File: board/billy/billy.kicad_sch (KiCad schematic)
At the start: 85 parts, among them J1 Screw_Terminal_01x02, J10 Screw_Terminal_01x02, J11 Screw_Terminal_01x03, J12 USB_B_Micro, J2 Conn_01x06, J3 Screw_Terminal_01x02, J4 Screw_Terminal_01x02, J5 Conn_01x02, J6 Conn_01x03, J7 Screw_Terminal_01x02, J8 Screw_Terminal_01x02, J9 Screw_Terminal_01x02, Q1 AOSS32334C, Q2 AOSS32334C, Q3 AOSS32334C, Q4 AOSS32334C, SW1 TS-1088-AR02016, U1 ESP32-S3-WROOM-1, U2 DRV8833PWPR, U3 MAX98357A, U4 DRV8833PWPR, U5 LM74700-Q1, U6 AP63201WU, U7 USBLC6-2SC6, U8 LM74700-Q1, U9 LM74700-Q1

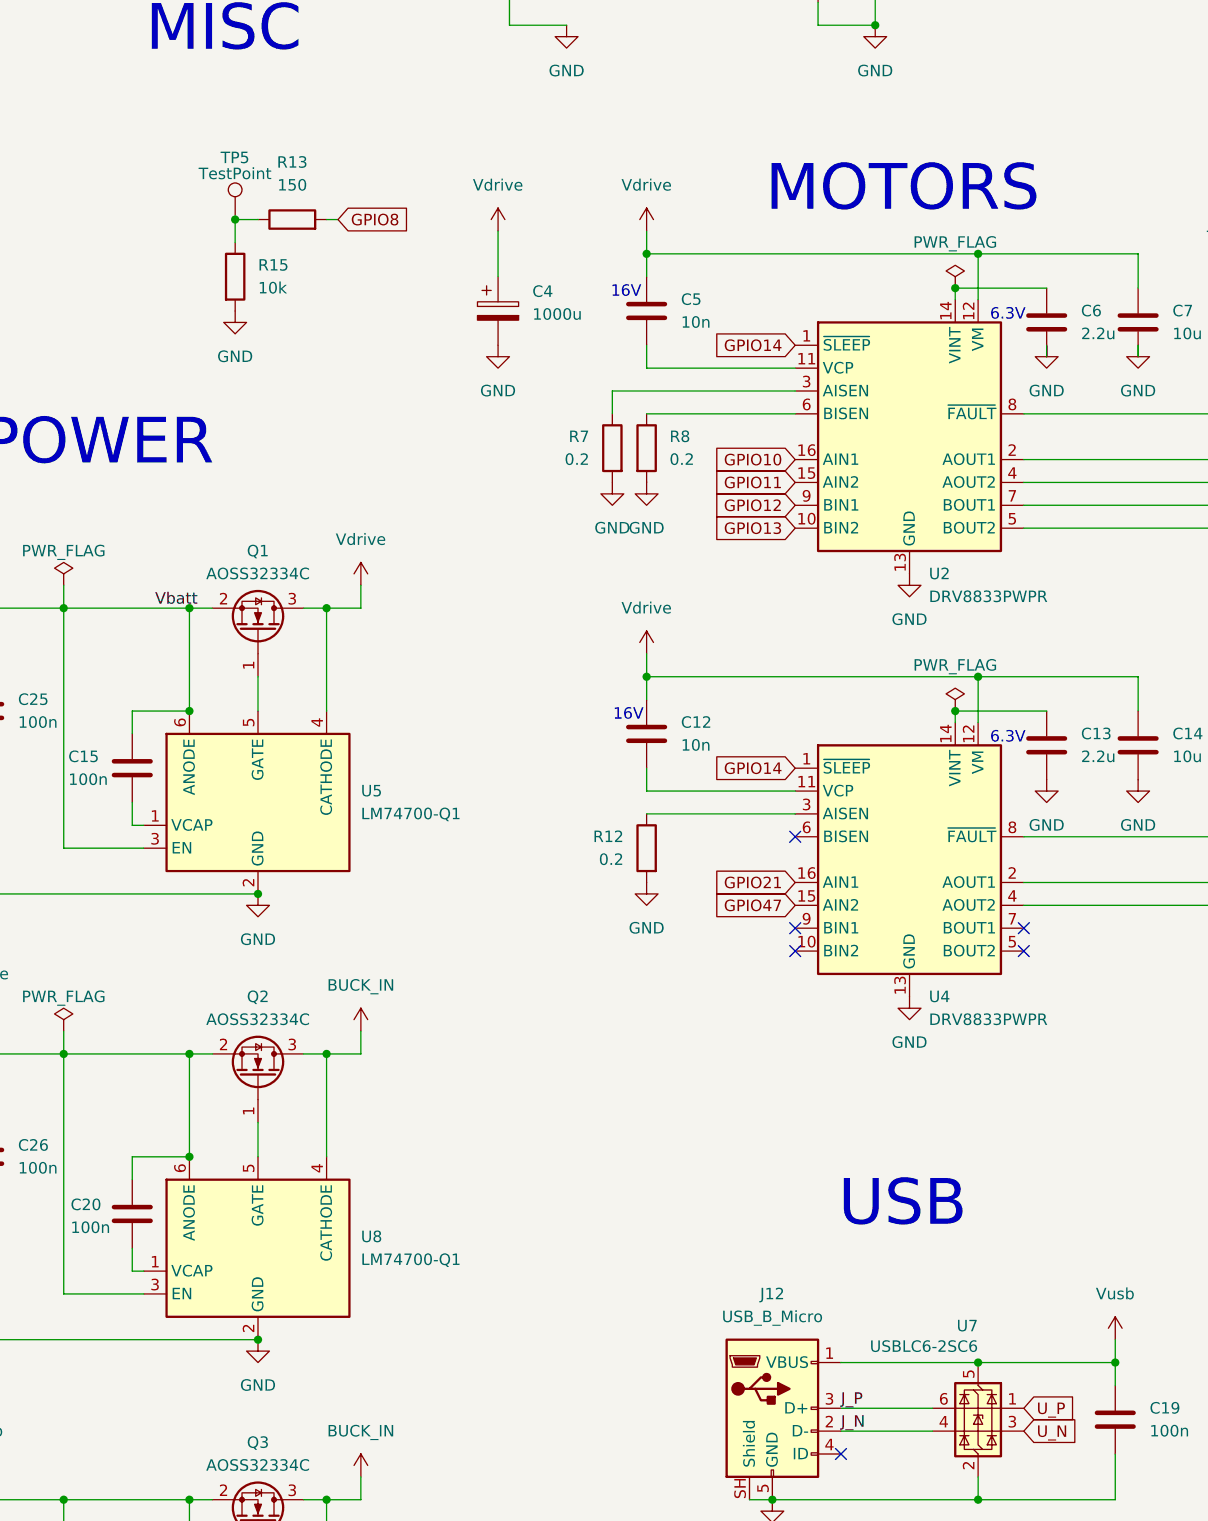
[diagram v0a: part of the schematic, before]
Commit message: Replace bare-pin misc probe (J13) with Keystone 5011 loop test point (TP5)
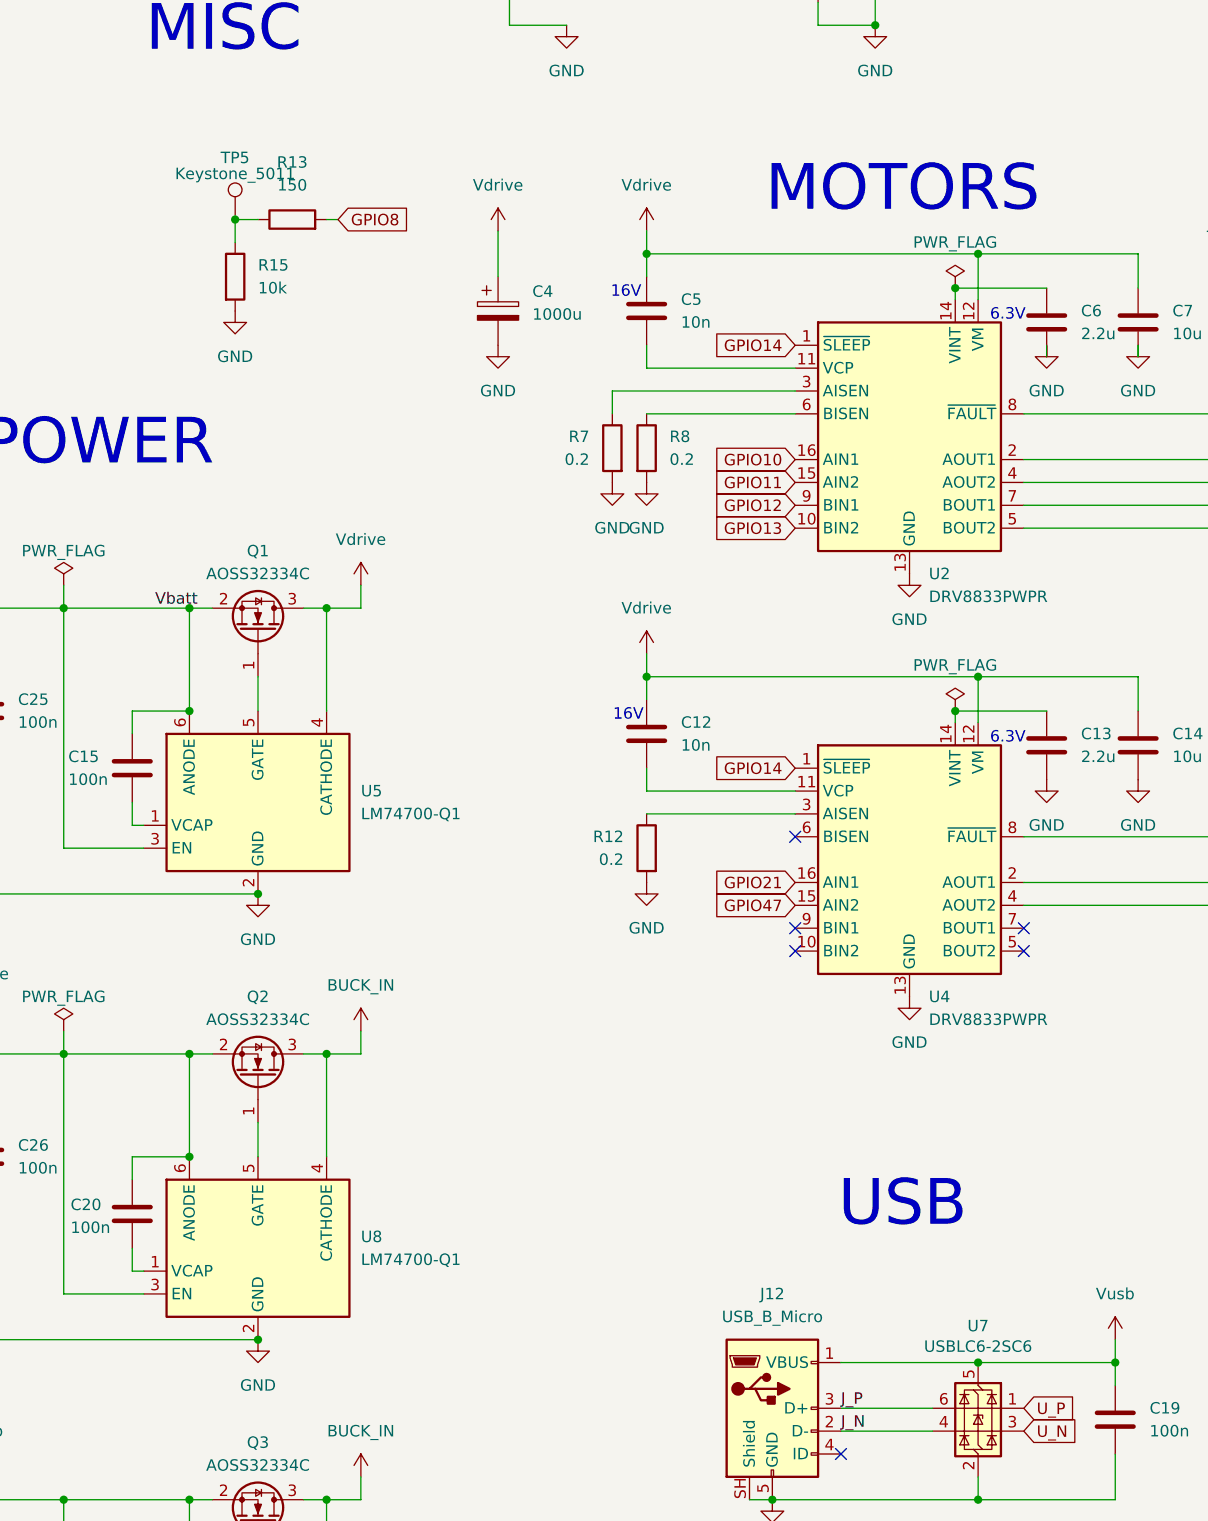
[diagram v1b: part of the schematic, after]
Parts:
- C1, C2, C3: DigiKey MF (none) -> Samsung Electro-Mechanics; DigiKey MP (none) -> CL05A105KA5NQNC
- C12, C5: DigiKey MF (none) -> Samsung Electro-Mechanics; DigiKey MP (none) -> CL05B103KB5NNNC
- C13, C6: DigiKey MF (none) -> Samsung Electro-Mechanics; DigiKey MP (none) -> CL10A225KO8NNNC
- C14, C7, C8: DigiKey MF (none) -> Samsung Electro-Mechanics; DigiKey MP (none) -> CL10A106KP8NNNC
- C15, C18, C19, C20, C21, C22, C25, C26, C27, C9: DigiKey MF (none) -> Samsung Electro-Mechanics; DigiKey MP (none) -> CL05B104KO5NNNC
- C16, C24: DigiKey MP CL21A226MAYNNWE -> CL21A226MAQNNNE
- C17: DigiKey MF (none) -> Samsung Electro-Mechanics; DigiKey MP (none) -> CL21A226MAQNNNE
- C4: DigiKey MF (none) -> PANASONIC; DigiKey MP (none) -> EEEFT1E102UP
- F1, F2: DigiKey MF (none) -> Littelfuse; DigiKey MP (none) -> 0154005.DRT
- J12: DigiKey MF (none) -> Amphenol ICC; DigiKey MP (none) -> 10118194-0001LF
- L1, L2: DigiKey MF (none) -> muRata; DigiKey MP (none) -> BLM18PG121SN1D
- Q1, Q2, Q3, Q4: DigiKey MF (none) -> AOS; DigiKey MP (none) -> AOSS32334C
- TP5: value TestPoint -> Keystone_5011; DigiKey MF (none) -> Keystone Electronics; DigiKey MP (none) -> 5011; DigiKey Part (none) -> 36-5011-ND; LCSC Part (none) -> C238127; MF (none) -> Keystone Electronics; MP (none) -> 5011
- U1: DigiKey MF (none) -> ESPRESSIF; DigiKey MP (none) -> ESP32-S3-WROOM-1-N4R2
- U2, U4: DigiKey MF (none) -> TI; DigiKey MP (none) -> DRV8833PWPR
- U3: DigiKey MF (none) -> MAXIM; DigiKey MP (none) -> MAX98357AETE+T
- U6: DigiKey MF (none) -> DIODES; DigiKey MP (none) -> AP63201WU-7
- U7: DigiKey MF (none) -> ST; DigiKey MP (none) -> USBLC6-2SC6

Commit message: Add part numbers for LM74700-Q1
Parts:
- U5, U8, U9: DigiKey MF (none) -> TI; DigiKey MP (none) -> LM74700QDBVTQ1; DigiKey Part (none) -> 296-53420-1-ND; LCSC Part (none) -> C2653623; MF (none) -> TI; MP (none) -> LM74700QDBVTQ1; Mouser MF (none) -> TI; Mouser MP (none) -> LM74700QDBVTQ1; Mouser Part (none) -> 595-LM74700QDBVTQ1

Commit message: Change some part numbers to active / in stock parts
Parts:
- C14, C7, C8: DigiKey MP CL10A106KP8NNNC -> CL10A106KP8NNND
- C16, C17, C24: DigiKey MP CL21A226MAQNNNE -> CL21A226KOQNNNG
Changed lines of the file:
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@@
 			)
 		)
-		(property "DigiKey MP" "CL10A106KP8NNNC"
+		(property "DigiKey MP" "CL10A106KP8NNND"
 			(at 256.54 97.79 0)
 			(hide yes)
@@
 			)
 		)
-		(property "DigiKey MP" "CL10A106KP8NNNC"
+		(property "DigiKey MP" "CL10A106KP8NNND"
 			(at 256.54 144.78 0)
 			(hide yes)
@@
 			)
 		)
-		(property "DigiKey MP" "CL10A106KP8NNNC"
+		(property "DigiKey MP" "CL10A106KP8NNND"
 			(at 330.2 110.49 0)
 			(hide yes)
@@
 			)
 		)
-		(property "DigiKey MP" "CL21A226MAQNNNE"
+		(property "DigiKey MP" "CL21A226KOQNNNG"
 			(at 309.88 201.93 0)
 			(hide yes)
@@
 			)
 		)
-		(property "DigiKey MP" "CL21A226MAQNNNE"
+		(property "DigiKey MP" "CL21A226KOQNNNG"
 			(at 379.73 201.93 0)
 			(hide yes)
@@
 			)
 		)
-		(property "DigiKey MP" "CL21A226MAQNNNE"
+		(property "DigiKey MP" "CL21A226KOQNNNG"
 			(at 391.16 201.93 0)
 			(hide yes)

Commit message: Open board rev.1, move over to using AP63203 part
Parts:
- removed C23: 100p, Capacitor_SMD:C_0402_1005Metric, symbol Device:C
- removed R14: 75k, Resistor_SMD:R_0603_1608Metric, symbol Device:R
- removed R16: 24k, Resistor_SMD:R_0603_1608Metric, symbol Device:R
- F1, F2: Mouser MF (none) -> Littelfuse; Mouser MP (none) -> 0154005.DRT; Mouser Part (none) -> 576-0154005.DRT
- J12: Mouser MF (none) -> Amphenol ICC; Mouser MP (none) -> 10118194-0001LF; Mouser Part (none) -> 649-10118194-0001LF
- L3: value 6.8u -> 3.3u; DigiKey MP TYA40206R8M-10 -> TYA40203R3M-10; DigiKey Part (none) -> 240-TYA40203R3M-10CT-ND; LCSC Part C6364812 -> (none); MF APV -> (none); MP ANR4030T6R8M -> (none); Mouser MF (none) -> Laird-Signal Integrity Products; Mouser MP (none) -> TYA40203R3M-10; Mouser Part (none) -> 739-TYA40203R3M-10
- TP5: Mouser MF (none) -> Keystone Electronics; Mouser MP (none) -> 5011; Mouser Part (none) -> 534-5011
- U6: value AP63201WU -> AP63203WU; symbol Regulator_Switching:AP63201WU -> Regulator_Switching:AP63203WU; DigiKey MP AP63201WU-7 -> AP63203WU-7; DigiKey Part (none) -> AP63203WU-7DICT-ND; LCSC Part C2071044 -> C780769; MP AP63201WU-7 -> AP63203WU-7; Mouser MF (none) -> DIODES; Mouser MP (none) -> AP63203QWU-7; Mouser Part (none) -> 621-AP63203QWU-7
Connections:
- net +3.3V: now also U6.1 (FB)
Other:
- note removed: "NOTE: We prefer AP63203 if available. If selected: 1. Remove 100p feed-forward cap 2. Remove voltage dividing resistors 3. Connect FB directly to +3.3V out 4. Inductor value 4.7uH"
- moved on the sheet: C16, C17, C22, C24, L3, U6

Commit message: Add Vmotor-sense divider on GPIO8 (R13/R15), shared across N8R8 dev and N4R2 main boards
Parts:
- removed TP5: Keystone_5011, TestPoint:TestPoint_Keystone_5010-5014_Multipurpose, symbol Connector:TestPoint
- R13: value 150 -> 100k; DigiKey MP RMCF0603FT150R -> RMCF0603FT100K; LCSC Part C22808 -> C25803; MP 0603WAF1500T5E -> 0603WAF1003T5E
- R15: value 10k -> 75k; DigiKey MP RMCF0603FT10K0 -> RMCF0603JT75K0; LCSC Part C25804 -> (none); MF UNI-ROYAL -> (none); MP 0603WAF1002T5E -> (none)
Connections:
- net GPIO8: now also R13.1, R15.1; no longer R13.2
- net Vdrive: now also R13.2
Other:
- note added: "V SENSE"
- note removed: "MISC"
- moved on the sheet: R13, R15

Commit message: Cleaned up the parts table and added Digikey and Mouser part numbers for all parts
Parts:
- C1, C2, C3: Attributes (none) -> 10% 25V X5R; DigiKey MF Samsung Electro-Mechanics -> (none); DigiKey MP CL05A105KA5NQNC -> (none); DigiKey Part (none) -> 1276-1445-1-ND; Mouser Part (none) -> 187-CL05A105KA5NQNC
- C10, C11: Attributes (none) -> 10% 50V X7R; DigiKey MF Vishay Vitramon -> (none); DigiKey MP VJ0402Y221KXACW1BC -> (none); DigiKey Part (none) -> 720-1616-1-ND; MF FH -> Vishay Vitramon; MP 0402B221K500NT -> VJ0402Y221KXACW1BC; Mouser Part (none) -> 77-VJ0402Y221KXACBC
- C12, C5: Attributes (none) -> 10% 50V X7R; DigiKey MF Samsung Electro-Mechanics -> (none); DigiKey MP CL05B103KB5NNNC -> (none); DigiKey Part (none) -> 1276-1028-1-ND; Mouser Part (none) -> 187-CL05B103KB5NNNC
- C13, C6: Attributes (none) -> 10% 16V X5R; DigiKey MF Samsung Electro-Mechanics -> (none); DigiKey MP CL10A225KO8NNNC -> (none); DigiKey Part (none) -> 1276-1040-1-ND; Mouser Part (none) -> 187-CL10A225KO8NNNC
- C14, C7, C8: Attributes (none) -> 10% 16V X5R; DigiKey MF Samsung Electro-Mechanics -> (none); DigiKey MP CL10A106KP8NNND -> (none); DigiKey Part (none) -> 1276-CL10A106KO8NQNCCT-ND; MP CL10A106KP8NNNC -> CL10A106KO8NQNC; Mouser Part (none) -> 187-CL10A106KO8NQNC
- C15, C18, C19, C20, C21, C22, C25, C26, C27, C9: Attributes (none) -> 10% 16V X7R; DigiKey MF Samsung Electro-Mechanics -> (none); DigiKey MP CL05B104KO5NNNC -> (none); DigiKey Part (none) -> 1276-1001-1-ND; Mouser Part (none) -> 187-CL05B104KO5NNNC
- C16, C17, C24: Attributes (none) -> 10% 16V X5R; DigiKey MF Samsung Electro-Mechanics -> (none); DigiKey MP CL21A226KOQNNNG -> (none); DigiKey Part (none) -> 1276-7092-1-ND; Mouser Part (none) -> 187-CL21A226MAQNNNE
- C4: Attributes (none) -> 20% 25V; DigiKey MF PANASONIC -> (none); DigiKey MP EEEFT1E102UP -> (none); DigiKey Part (none) -> P122428CT-ND; Mouser Part (none) -> 667-EEE-FT1E102UP
- D1: DigiKey MF SparkFun -> (none); DigiKey MP 16347 -> (none); DigiKey Part (none) -> 1568-16347CT-ND; MF Worldsemi -> SparkFun; MP WS2812B-V6 -> 16347
- F1, F2: DigiKey MF Littelfuse -> (none); DigiKey MP 0154005.DRT -> (none); DigiKey Part (none) -> F1310CT-ND
- J1, J10, J3, J4, J7, J8, J9: DigiKey MF Phoenix Contact -> (none); DigiKey MP 1725656 -> (none); DigiKey Part (none) -> 277-1273-ND; MF DORABO -> Phoenix Contact; MP DB125-2.54-2P-GN-S -> 1725656; Mouser Part (none) -> 651-1725656
- J11: DigiKey MF Phoenix Contact -> (none); DigiKey MP 1725669 -> (none); DigiKey Part (none) -> 277-1274-ND; MF DORABO -> Phoenix Contact; MP DB125-2.54-3P-GN-S -> 1725669; Mouser Part (none) -> 651-1725669
- J12: DigiKey MF Amphenol ICC -> (none); DigiKey MP 10118194-0001LF -> (none); DigiKey Part (none) -> 609-4618-1-ND
- J2: DigiKey MF Würth Elektronik -> (none); DigiKey MP 61300611021 -> (none); DigiKey Part (none) -> 732-5339-ND; MF XFCN -> Würth Elektronik; MP PZ254R-11-06P -> 61300611021; Mouser Part (none) -> 710-61300611021
- J5: DigiKey MF Würth Elektronik -> (none); DigiKey MP 61300211121 -> (none); DigiKey Part (none) -> 732-5315-ND; MF XFCN -> Würth Elektronik; MP PZ254V-11-02P -> 61300211121; Mouser Part (none) -> 710-61300211121
- J6: DigiKey MF Würth Elektronik -> (none); DigiKey MP 61300311121 -> (none); DigiKey Part (none) -> 732-5316-ND; MF XFCN -> Würth Elektronik; MP PZ254V-11-03P -> 61300311121; Mouser Part (none) -> 710-61300311121
- L1, L2: value 50m -> 30m; DigiKey MF muRata -> (none); DigiKey MP BLM18PG121SN1D -> (none); DigiKey Part (none) -> 490-5254-1-ND; MP BLM18PG121SN1D -> BLM18KG121TN1D; Mouser Part (none) -> 81-BLM18KG121TN1D
- L3: DigiKey MF Laird-Signal Integrity Products -> (none); DigiKey MP TYA40203R3M-10 -> (none); MF (none) -> Laird-Signal Integrity Products; MP (none) -> TYA40203R3M-10
- Q1, Q2, Q3, Q4: DigiKey MF AOS -> (none); DigiKey MP AOSS32334C -> (none); DigiKey Part (none) -> 785-AOSS32334CCT-ND
- R1, R18, R2, R3, R4, R5, R6: Attributes (none) -> 1% 0.1W 100ppm; DigiKey MF Stackpole Electronics -> (none); DigiKey MP RMCF0603FT10K0 -> (none); DigiKey Part (none) -> RMCF0603FT10K0CT-ND; MF UNI-ROYAL -> Stackpole Electronics; MP 0603WAF1002T5E -> RMCF0603FT10K0; Mouser Part (none) -> 708-RMCF0603FT10K0
- R10, R13, R9: Attributes (none) -> 1% 0.1W 100ppm; DigiKey MF Stackpole Electronics -> (none); DigiKey MP RMCF0603FT100K -> (none); DigiKey Part (none) -> RMCF0603FT100KCT-ND; MF UNI-ROYAL -> Stackpole Electronics; MP 0603WAF1003T5E -> RMCF0603FT100K; Mouser Part (none) -> 708-RMCF0603FT100K
- R12, R7, R8: Attributes (none) -> 1% 0.5W 100ppm; DigiKey MF Stackpole Electronics -> (none); DigiKey MP CSR1206FKR200 -> (none); DigiKey Part (none) -> CSR1206FKR200CT-ND; MF UNI-ROYAL -> Stackpole Electronics; MP HP06W2F200LT5E -> CSR1206FKR200; Mouser Part (none) -> 708-CSR1206FKR200
- R15: Attributes (none) -> 1% 0.1W 100ppm; DigiKey MF Stackpole Electronics -> (none); DigiKey MP RMCF0603JT75K0 -> (none); DigiKey Part (none) -> RMCF0603FT75K0CT-ND; MF (none) -> Stackpole Electronics; MP (none) -> RMCF0603FT75K0; Mouser Part (none) -> 708-RMCF0603FT75K0
- R17: Attributes (none) -> 1% 0.1W 100ppm; DigiKey MF Stackpole Electronics -> (none); DigiKey MP RMCF0603FT470R -> (none); DigiKey Part (none) -> RMCF0603FT470RCT-ND; MF UNI-ROYAL -> Stackpole Electronics; MP 0603WAF4700T5E -> RMCF0603FT470R; Mouser Part (none) -> 708-RMCF0603FT470R
- SW1: DigiKey MF Alps Alpine -> (none); DigiKey MP SKRKAGE020 -> (none); DigiKey Part (none) -> 4809-SKRKAGE020CT-ND; MF XUNPU -> Alps Alpine; MP TS-1088-AR02016 -> SKRKAGE020; Mouser Part (none) -> 688-SKRKAG
- U1: DigiKey MF ESPRESSIF -> (none); DigiKey MP ESP32-S3-WROOM-1-N4R2 -> (none); DigiKey Part (none) -> 5407-ESP32-S3-WROOM-1-N4R2CT-ND; Mouser Part (none) -> 356-ESP32S3WROM1N4R2
- U2, U4: DigiKey MF TI -> (none); DigiKey MP DRV8833PWPR -> (none); DigiKey Part (none) -> 296-29434-1-ND; Mouser Part (none) -> 595-DRV8833PWPR
- U3: DigiKey MF MAXIM -> (none); DigiKey MP MAX98357AETE+T -> (none); DigiKey Part (none) -> MAX98357AETE+TCT-ND; Mouser Part (none) -> 700-MAX98357AETE+T
- U5, U8, U9: DigiKey MF TI -> (none); DigiKey MP LM74700QDBVTQ1 -> (none)
- U6: DigiKey MF DIODES -> (none); DigiKey MP AP63203WU-7 -> (none)
- U7: DigiKey MF ST -> (none); DigiKey MP USBLC6-2SC6 -> (none); DigiKey Part (none) -> 497-5235-1-ND; Mouser Part (none) -> 511-USBLC6-2SC6

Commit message: Rev 1 board updates
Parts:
- added TP5, TP6: TestPoint, TestPoint:TestPoint_Pad_1.0x1.0mm, symbol Connector:TestPoint
- C1, C2, C3: footprint Capacitor_SMD:C_0402_1005Metric -> Capacitor_SMD:C_0603_1608Metric; Attributes 10% 25V X5R -> 10% 10V X7R; DigiKey Part 1276-1445-1-ND -> 1276-1946-1-ND; MP CL05A105KA5NQNC -> CL10B105KP8NNNC; Mouser Part 187-CL05A105KA5NQNC -> 187-CL10B105KP8NNNC
- C10, C11: footprint Capacitor_SMD:C_0402_1005Metric -> Capacitor_SMD:C_0603_1608Metric; DigiKey Part 720-1616-1-ND -> 1276-1145-1-ND; MF Vishay Vitramon -> Samsung Electro-Mechanics; MP VJ0402Y221KXACW1BC -> CL10B221KB8NNNC; Mouser Part 77-VJ0402Y221KXACBC -> 187-CL10B221KB8NNNC
- C12, C5: footprint Capacitor_SMD:C_0402_1005Metric -> Capacitor_SMD:C_0603_1608Metric
- C13, C6: Attributes 10% 16V X5R -> 10% 10V X5R; DigiKey Part 1276-1040-1-ND -> 1276-1085-1-ND; MP CL10A225KO8NNNC -> CL10A225KP8NNNC; Mouser Part 187-CL10A225KO8NNNC -> 187-CL10A225KP8NNNC
- C14, C7, C8: Attributes 10% 16V X5R -> 10% 10V X5R; DigiKey Part 1276-CL10A106KO8NQNCCT-ND -> 1276-1192-1-ND; MP CL10A106KO8NQNC -> CL10A106KP8NNNC; Mouser Part 187-CL10A106KO8NQNC -> 187-CL10A106KP8NNNC
- C15, C18, C19, C20, C21, C22, C25, C26, C27, C9: footprint Capacitor_SMD:C_0402_1005Metric -> Capacitor_SMD:C_0603_1608Metric; Attributes 10% 16V X7R -> 5% 50V X7R; DigiKey Part 1276-1001-1-ND -> 1276-1033-1-ND; MP CL05B104KO5NNNC -> CL10B104JB8NNNC; Mouser Part 187-CL05B104KO5NNNC -> 187-CL10B104JB8NNNC
- C16, C24: footprint Capacitor_SMD:C_0805_2012Metric -> Capacitor_SMD:C_1206_3216Metric; Attributes 10% 16V X5R -> 10% 10V X7R; DigiKey Part 1276-7092-1-ND -> 1276-2769-1-ND; MP CL21A226MAQNNNE -> CL31B226KPHNNNE; Mouser Part 187-CL21A226MAQNNNE -> 187-CL31B226KPHNNNE
- C17: value 22u -> 10u; footprint Capacitor_SMD:C_0805_2012Metric -> Capacitor_SMD:C_1206_3216Metric; Attributes 10% 16V X5R -> 10% 35V X7R; DigiKey Part 1276-7092-1-ND -> 1276-3103-1-ND; MP CL21A226MAQNNNE -> CL31B106KLHNNNE; Mouser Part 187-CL21A226MAQNNNE -> 187-CL31B106KLHNNNE
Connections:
- net Vbatt: now also TP5.1
- net Vusb: now also TP6.1
